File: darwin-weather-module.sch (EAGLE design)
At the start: 24 parts, among them J1 2X6-HEADERS, J2 95501-6889VERT, U2 ATSAMD09, U3 M24C02-WMN6TP, U4 PCA9615

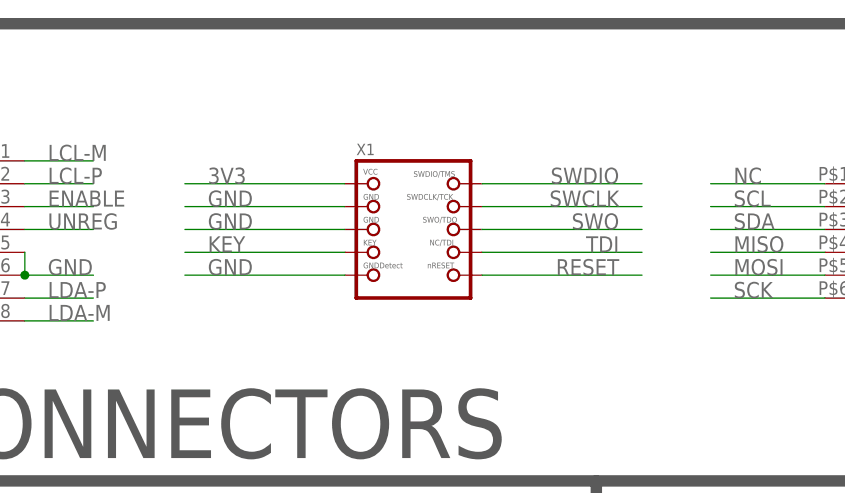
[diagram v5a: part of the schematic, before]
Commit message: Migrated programming header to Tag-Connect.
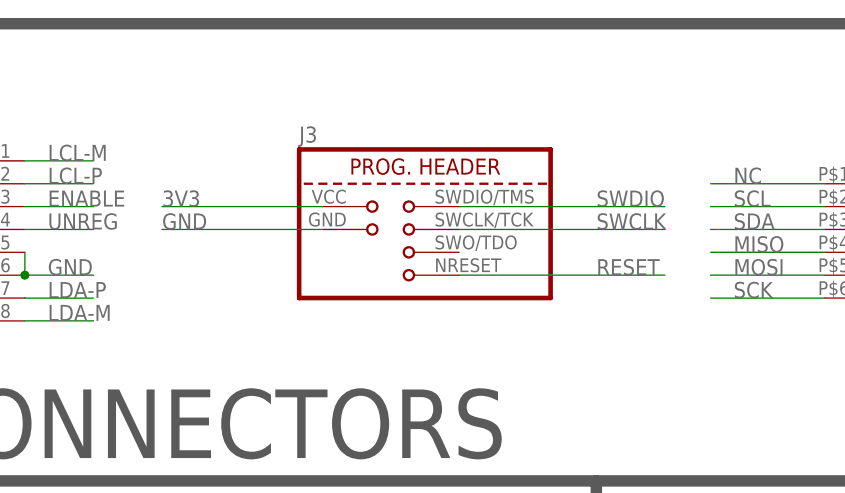
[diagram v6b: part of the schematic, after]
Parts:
- removed X1: (no value), microbuilder:JTAG-CORTEXBOX
- added J3: TAG-CONNECT, Conservify:TAG-CONNECT
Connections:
- removed net KEY: X1.KEY
- removed net SWO: X1.SWO
- removed net TDI: X1.TDI
- net 3V3: now also J3.VCC; no longer X1.VCC
- net GND: now also J3.GND; no longer X1.GND@1, X1.GND@2, X1.GNDDETECT
- net RESET: now also J3.RESET; no longer X1.NRESET
- net SWCLK: now also J3.SWCLK; no longer X1.SWDCLK
- net SWDIO: now also J3.SWDIO; no longer X1.SWDIO
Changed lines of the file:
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@@
 <?xml version="1.0" encoding="utf-8"?>
 <!DOCTYPE eagle SYSTEM "eagle.dtd">
-<eagle version="9.5.0">
+<eagle version="9.6.1">
 <drawing>
 <settings>
@@
 <layer number="1" name="Top" color="4" fill="1" visible="no" active="no"/>
 <layer number="2" name="Route2" color="16" fill="1" visible="no" active="no"/>
+<layer number="3" name="Route3" color="4" fill="3" visible="no" active="no"/>
+<layer number="4" name="Route4" color="1" fill="4" visible="no" active="no"/>
+<layer number="5" name="Route5" color="4" fill="4" visible="no" active="no"/>
+<layer number="6" name="Route6" color="1" fill="8" visible="no" active="no"/>
+<layer number="7" name="Route7" color="4" fill="8" visible="no" active="no"/>
+<layer number="8" name="Route8" color="1" fill="2" visible="no" active="no"/>
+<layer number="9" name="Route9" color="4" fill="2" visible="no" active="no"/>
+<layer number="10" name="Route10" color="1" fill="7" visible="no" active="no"/>
+<layer number="11" name="Route11" color="4" fill="7" visible="no" active="no"/>
+<layer number="12" name="Route12" color="1" fill="5" visible="no" active="no"/>
+<layer number="13" name="Route13" color="4" fill="5" visible="no" active="no"/>
+<layer number="14" name="Route14" color="1" fill="6" visible="no" active="no"/>
 <layer number="15" name="Route15" color="23" fill="1" visible="no" active="no"/>
 <layer number="16" name="Bottom" color="1" fill="1" visible="no" active="no"/>
@@
 <part name="C9" library="rcl" library_urn="urn:adsk.eagle:library:334" deviceset="C-US" device="C0603K" package3d_urn="urn:adsk.eagle:package:23680/2" value=".1uf"/>
 <part name="R1" library="SparkFun-Resistors" library_urn="urn:adsk.eagle:library:532" deviceset="100KOHM" device="-0603-1/10W-1%" package3d_urn="urn:adsk.eagle:package:39650/1" value="100k"/>
-<part name="X1" library="microbuilder" deviceset="JTAG-CORTEX" device="BOX"/>
 <part name="U3" library="Conservify" library_urn="urn:adsk.eagle:library:11839183" deviceset="M24C02-WMN6TP" device="" package3d_urn="urn:adsk.eagle:package:12022475/1"/>
 <part name="J2" library="Conservify" library_urn="urn:adsk.eagle:library:11839183" deviceset="95501-6889" device="VERT" package3d_urn="urn:adsk.eagle:package:12024212/2"/>
@@
 <part name="R10" library="SparkFun-Resistors" library_urn="urn:adsk.eagle:library:532" deviceset="100KOHM" device="-0603-1/10W-1%" package3d_urn="urn:adsk.eagle:package:39650/1" value="4.7k"/>
 <part name="R11" library="SparkFun-Resistors" library_urn="urn:adsk.eagle:library:532" deviceset="100KOHM" device="-0603-1/10W-1%" package3d_urn="urn:adsk.eagle:package:39650/1" value="4.7k"/>
+<part name="J3" library="Conservify" library_urn="urn:adsk.eagle:library:11839183" deviceset="TAG-CONNECT" device="" package3d_urn="urn:adsk.eagle:package:16969550/1"/>
 </parts>
 <sheets>
@@
 <attribute name="VALUE" x="65.024" y="-2.54" size="1.778" layer="96" font="vector" rot="R90" align="top-center"/>
 </instance>
-<instance part="X1" gate="G$1" x="99.06" y="91.44" smashed="yes">
-<attribute name="NAME" x="92.71" y="99.695" size="1.27" layer="95"/>
-<attribute name="VALUE" x="92.71" y="81.915" size="1.27" layer="96"/>
-</instance>
 <instance part="U3" gate="G$1" x="162.56" y="-7.62" smashed="yes">
 <attribute name="NAME" x="149.86" y="5.334" size="1.778" layer="95"/>
@@
 <attribute name="NAME" x="218.44" y="61.976" size="1.778" layer="95" font="vector" rot="R180" align="bottom-center"/>
 <attribute name="VALUE" x="218.44" y="65.024" size="1.778" layer="96" font="vector" rot="R180" align="top-center"/>
+</instance>
+<instance part="J3" gate="G$1" x="96.52" y="91.44" smashed="yes">
+<attribute name="NAME" x="86.36" y="101.092" size="1.778" layer="95"/>
 </instance>
 </instances>
@@
 </segment>
 <segment>
-<pinref part="X1" gate="G$1" pin="GND@1"/>
-<wire x1="91.44" y1="93.98" x2="73.66" y2="93.98" width="0.1524" layer="91"/>
-<label x="76.2" y="93.98" size="1.778" layer="95"/>
-</segment>
-<segment>
-<pinref part="X1" gate="G$1" pin="GND@2"/>
-<wire x1="91.44" y1="91.44" x2="73.66" y2="91.44" width="0.1524" layer="91"/>
-<label x="76.2" y="91.44" size="1.778" layer="95"/>
-</segment>
-<segment>
-<pinref part="X1" gate="G$1" pin="GNDDETECT"/>
-<wire x1="91.44" y1="86.36" x2="73.66" y2="86.36" width="0.1524" layer="91"/>
-<label x="76.2" y="86.36" size="1.778" layer="95"/>
-</segment>
-<segment>
 <pinref part="U2" gate="G$1" pin="GND"/>
 <wire x1="58.42" y1="50.8" x2="45.72" y2="50.8" width="0.1524" layer="91"/>
@@
 <label x="241.3" y="27.94" size="1.778" layer="95"/>
 </segment>
+<segment>
+<pinref part="J3" gate="G$1" pin="GND"/>
+<wire x1="88.9" y1="91.44" x2="71.12" y2="91.44" width="0.2032" layer="91"/>
+<label x="71.12" y="91.44" size="1.778" layer="95"/>
+</segment>
 </net>
 <net name="3V3" class="0">
@@
 </segment>
 <segment>
-<pinref part="X1" gate="G$1" pin="VCC"/>
-<wire x1="91.44" y1="96.52" x2="73.66" y2="96.52" width="0.1524" layer="91"/>
-<label x="76.2" y="96.52" size="1.778" layer="95"/>
-</segment>
-<segment>
 <pinref part="U2" gate="G$1" pin="VDD"/>
 <wire x1="58.42" y1="53.34" x2="45.72" y2="53.34" width="0.1524" layer="91"/>
@@
 <label x="228.6" y="68.58" size="1.778" layer="95"/>
 </segment>
+<segment>
+<pinref part="J3" gate="G$1" pin="VCC"/>
+<wire x1="88.9" y1="93.98" x2="71.12" y2="93.98" width="0.2032" layer="91"/>
+<label x="71.12" y="93.98" size="1.778" layer="95"/>
+</segment>
 </net>
 <net name="N$6" class="0">
@@
 <net name="SWCLK" class="0">
 <segment>
-<pinref part="X1" gate="G$1" pin="SWDCLK"/>
-<wire x1="106.68" y1="93.98" x2="124.46" y2="93.98" width="0.1524" layer="91"/>
-<label x="121.92" y="93.98" size="1.778" layer="95" align="bottom-right"/>
-</segment>
-<segment>
 <pinref part="U2" gate="G$1" pin="PA30"/>
 <wire x1="93.98" y1="27.94" x2="106.68" y2="27.94" width="0.1524" layer="91"/>
 <label x="99.06" y="27.94" size="1.778" layer="95"/>
 </segment>
+<segment>
+<pinref part="J3" gate="G$1" pin="SWCLK"/>
+<wire x1="104.14" y1="91.44" x2="127" y2="91.44" width="0.2032" layer="91"/>
+<label x="119.38" y="91.44" size="1.778" layer="95"/>
+</segment>
 </net>
 <net name="SWDIO" class="0">
-<segment>
-<pinref part="X1" gate="G$1" pin="SWDIO"/>
-<wire x1="106.68" y1="96.52" x2="124.46" y2="96.52" width="0.1524" layer="91"/>
-<label x="121.92" y="96.52" size="1.778" layer="95" align="bottom-right"/>
-</segment>
 <segment>
 <pinref part="U2" gate="G$1" pin="PA31"/>
@@
 <label x="99.06" y="25.4" size="1.778" layer="95"/>
 </segment>
+<segment>
+<pinref part="J3" gate="G$1" pin="SWDIO"/>
+<wire x1="104.14" y1="93.98" x2="127" y2="93.98" width="0.2032" layer="91"/>
+<label x="119.38" y="93.98" size="1.778" layer="95"/>
+</segment>
 </net>
 <net name="RESET" class="0">
-<segment>
-<pinref part="X1" gate="G$1" pin="NRESET"/>
-<wire x1="106.68" y1="86.36" x2="124.46" y2="86.36" width="0.1524" layer="91"/>
-<label x="121.92" y="86.36" size="1.778" layer="95" align="bottom-right"/>
-</segment>
 <segment>
 <pinref part="U2" gate="G$1" pin="PA28/!RESET"/>
@@
 <label x="99.06" y="30.48" size="1.778" layer="95"/>
 </segment>
-</net>
-<net name="KEY" class="0">
-<segment>
-<pinref part="X1" gate="G$1" pin="KEY"/>
-<wire x1="91.44" y1="88.9" x2="73.66" y2="88.9" width="0.1524" layer="91"/>
-<label x="76.2" y="88.9" size="1.778" layer="95"/>
-</segment>
-</net>
-<net name="SWO" class="0">
-<segment>
-<pinref part="X1" gate="G$1" pin="SWO"/>
-<wire x1="106.68" y1="91.44" x2="124.46" y2="91.44" width="0.1524" layer="91"/>
-<label x="121.92" y="91.44" size="1.778" layer="95" align="bottom-right"/>
-</segment>
-</net>
-<net name="TDI" class="0">
-<segment>
-<pinref part="X1" gate="G$1" pin="TDI"/>
-<wire x1="106.68" y1="88.9" x2="124.46" y2="88.9" width="0.1524" layer="91"/>
-<label x="121.92" y="88.9" size="1.778" layer="95" align="bottom-right"/>
-</segment>
-</net>
+<segment>
+<pinref part="J3" gate="G$1" pin="RESET"/>
+<wire x1="104.14" y1="86.36" x2="127" y2="86.36" width="0.2032" layer="91"/>
+<label x="119.38" y="86.36" size="1.778" layer="95"/>
+</segment>
+</net>
